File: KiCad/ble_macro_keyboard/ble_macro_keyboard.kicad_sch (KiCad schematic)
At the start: 34 parts, among them IC1 ADP3338AKCZ-3.3-RL, J1 Conn_01x03_Male, Q1 IRLML6402, SW1 SW_SPDT, SW10 SW_Push, SW11 SW_Push, SW12 SW_Push, SW13 SW_Push, SW14 SW_Push, SW2 SW_Push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

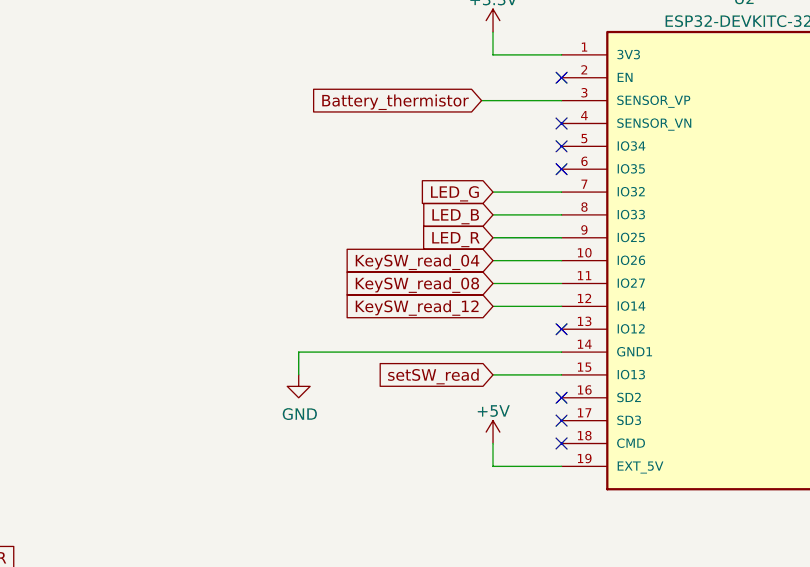
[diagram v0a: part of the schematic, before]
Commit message: [fix] Ble_keyboardフットプリントライブラリのSWがGNDに接続するように解決
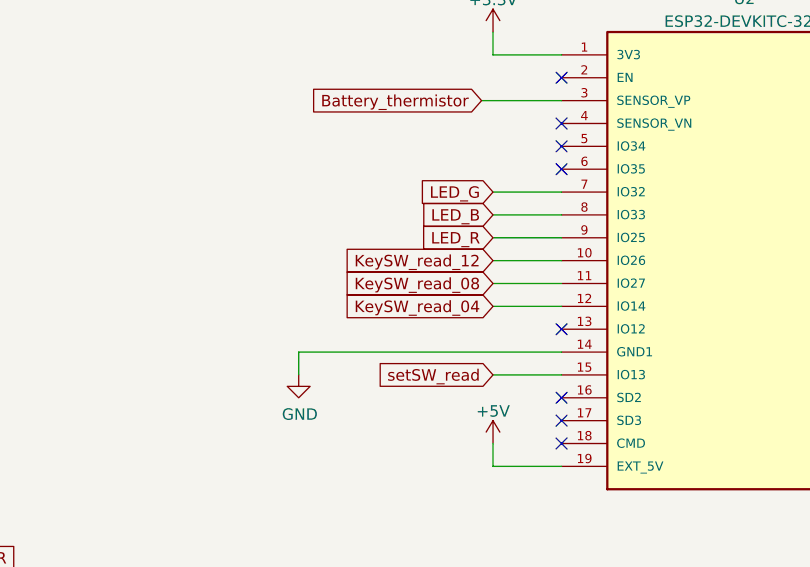
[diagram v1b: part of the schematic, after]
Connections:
- net KeySW_read_04: now also U2.12 (IO14); no longer U2.10 (IO26)
- net KeySW_read_12: now also U2.10 (IO26); no longer U2.12 (IO14)
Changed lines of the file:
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@@
+    (stroke (width 0) (type default) (color 0 0 0 0))
+  )
+  (wire (pts (xy 175.26 50.8) (xy 182.88 50.8))
+    (stroke (width 0) (type default) (color 0 0 0 0))
+  )
+  (wire (pts (xy 195.58 119.38) (xy 203.2 119.38))
+    (stroke (width 0) (type default) (color 0 0 0 0))
+  )
+  (wire (pts (xy 149.86 66.04) (xy 152.4 66.04))
+    (stroke (width 0) (type default) (color 0 0 0 0))
+  )
+  (wire (pts (xy 38.1 25.4) (xy 38.1 46.99))
+    (stroke (width 0) (type default) (color 0 0 0 0))
+  )
+  (wire (pts (xy 76.2 45.72) (xy 73.66 45.72))
+    (stroke (width 0) (type default) (color 0 0 0 0))
+  )
+  (wire (pts (xy 101.6 139.7) (xy 109.22 139.7))
+    (stroke (width 0) (type default) (color 0 0 0 0))
+  )
+  (wire (pts (xy 63.5 59.69) (xy 63.5 50.8))
+    (stroke (width 0) (type default) (color 0 0 0 0))
+  )
+  (wire (pts (xy 101.6 101.6) (xy 109.22 101.6))
+    (stroke (width 0) (type default) (color 0 0 0 0))
+  )
+  (wire (pts (xy 243.84 142.24) (xy 250.19 142.24))
+    (stroke (width 0) (type default) (color 0 0 0 0))
+  )
+  (wire (pts (xy 182.88 67.31) (xy 182.88 76.2))
+    (stroke (width 0) (type default) (color 0 0 0 0))
+  )
+  (wire (pts (xy 182.88 50.8) (xy 218.44 50.8))
+    (stroke (width 0) (type default) (color 0 0 0 0))
+  )
+  (wire (pts (xy 127 45.72) (xy 111.76 45.72))
+    (stroke (width 0) (type default) (color 0 0 0 0))
+  )
+  (wire (pts (xy 243.84 132.08) (xy 250.19 132.08))
     (stroke (width 0) (type default) (color 0 0 0 0))
   )
@@
     (stroke (width 0) (type default) (color 0 0 0 0))
   )
-  (wire (pts (xy 175.26 50.8) (xy 182.88 50.8))
-    (stroke (width 0) (type default) (color 0 0 0 0))
-  )
-  (wire (pts (xy 195.58 119.38) (xy 203.2 119.38))
-    (stroke (width 0) (type default) (color 0 0 0 0))
-  )
-  (wire (pts (xy 149.86 66.04) (xy 152.4 66.04))
-    (stroke (width 0) (type default) (color 0 0 0 0))
-  )
-  (wire (pts (xy 38.1 25.4) (xy 38.1 46.99))
-    (stroke (width 0) (type default) (color 0 0 0 0))
-  )
-  (wire (pts (xy 76.2 45.72) (xy 73.66 45.72))
-    (stroke (width 0) (type default) (color 0 0 0 0))
-  )
-  (wire (pts (xy 101.6 139.7) (xy 109.22 139.7))
-    (stroke (width 0) (type default) (color 0 0 0 0))
-  )
-  (wire (pts (xy 63.5 59.69) (xy 63.5 50.8))
-    (stroke (width 0) (type default) (color 0 0 0 0))
-  )
-  (wire (pts (xy 101.6 101.6) (xy 109.22 101.6))
-    (stroke (width 0) (type default) (color 0 0 0 0))
-  )
-  (wire (pts (xy 243.84 142.24) (xy 250.19 142.24))
-    (stroke (width 0) (type default) (color 0 0 0 0))
-  )
-  (wire (pts (xy 182.88 67.31) (xy 182.88 76.2))
-    (stroke (width 0) (type default) (color 0 0 0 0))
-  )
-  (wire (pts (xy 182.88 50.8) (xy 218.44 50.8))
-    (stroke (width 0) (type default) (color 0 0 0 0))
-  )
-  (wire (pts (xy 127 45.72) (xy 111.76 45.72))
-    (stroke (width 0) (type default) (color 0 0 0 0))
-  )
-  (wire (pts (xy 243.84 132.08) (xy 250.19 132.08))
-    (stroke (width 0) (type default) (color 0 0 0 0))
-  )
   (wire (pts (xy 195.58 149.86) (xy 195.58 147.32))
     (stroke (width 0) (type default) (color 0 0 0 0))
@@
     (stroke (width 0) (type default) (color 0 0 0 0))
   )
+  (wire (pts (xy 195.58 129.54) (xy 203.2 129.54))
+    (stroke (width 0) (type default) (color 0 0 0 0))
+  )
+  (wire (pts (xy 38.1 101.6) (xy 45.72 101.6))
+    (stroke (width 0) (type default) (color 0 0 0 0))
+  )
+  (wire (pts (xy 119.38 88.9) (xy 127 88.9))
+    (stroke (width 0) (type default) (color 0 0 0 0))
+  )
+  (wire (pts (xy 38.1 165.1) (xy 45.72 165.1))
+    (stroke (width 0) (type default) (color 0 0 0 0))
+  )
+  (wire (pts (xy 243.84 134.62) (xy 250.19 134.62))
+    (stroke (width 0) (type default) (color 0 0 0 0))
+  )
+  (wire (pts (xy 38.1 152.4) (xy 45.72 152.4))
+    (stroke (width 0) (type default) (color 0 0 0 0))
+  )
   (wire (pts (xy 195.58 127) (xy 203.2 127))
-    (stroke (width 0) (type default) (color 0 0 0 0))
-  )
-  (wire (pts (xy 195.58 129.54) (xy 203.2 129.54))
-    (stroke (width 0) (type default) (color 0 0 0 0))
-  )
-  (wire (pts (xy 38.1 101.6) (xy 45.72 101.6))
-    (stroke (width 0) (type default) (color 0 0 0 0))
-  )
-  (wire (pts (xy 119.38 88.9) (xy 127 88.9))
-    (stroke (width 0) (type default) (color 0 0 0 0))
-  )
-  (wire (pts (xy 38.1 165.1) (xy 45.72 165.1))
-    (stroke (width 0) (type default) (color 0 0 0 0))
-  )
-  (wire (pts (xy 243.84 134.62) (xy 250.19 134.62))
-    (stroke (width 0) (type default) (color 0 0 0 0))
-  )
-  (wire (pts (xy 38.1 152.4) (xy 45.72 152.4))
     (stroke (width 0) (type default) (color 0 0 0 0))
   )
@@
     )
   )
-  (global_label "KeySW_read_12" (shape input) (at 195.58 132.08 180) (fields_autoplaced)
-    (effects (font (size 1.27 1.27)) (justify right))
-    (property "Intersheet References" "${INTERSHEET_REFS}" (id 0) (at 178.7415 132.0006 0)
+  (global_label "KeySW_read_12" (shape input) (at 195.58 127 180) (fields_autoplaced)
+    (effects (font (size 1.27 1.27)) (justify right))
+    (property "Intersheet References" "${INTERSHEET_REFS}" (id 0) (at 178.7415 126.9206 0)
       (effects (font (size 1.27 1.27)) (justify right) hide)
     )
@@
     )
   )
-  (global_label "KeySW_read_04" (shape input) (at 195.58 127 180) (fields_autoplaced)
-    (effects (font (size 1.27 1.27)) (justify right))
-    (property "Intersheet References" "${INTERSHEET_REFS}" (id 0) (at 316.23 289.56 0)
-      (effects (font (size 1.27 1.27)) hide)
-    )
+  (global_label "KeySW_read_04" (shape input) (at 195.58 132.08 180) (fields_autoplaced)
+    (effects (font (size 1.27 1.27)) (justify right))
+    (property "Intersheet References" "${INTERSHEET_REFS}" (id 0) (at 316.23 294.64 0)
+      (effects (font (size 1.27 1.27)) hide)
+    )
